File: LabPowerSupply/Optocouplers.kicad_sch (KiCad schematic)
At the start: 3 parts

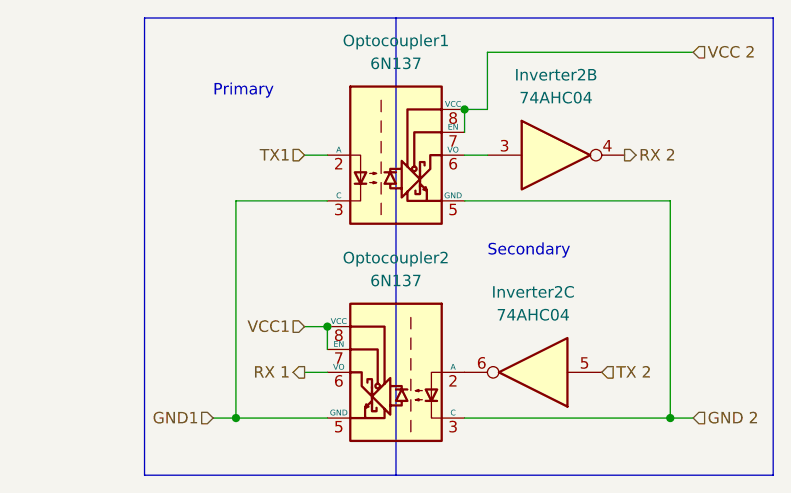
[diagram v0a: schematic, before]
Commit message: Fixed MCU communication pins and optocoupler
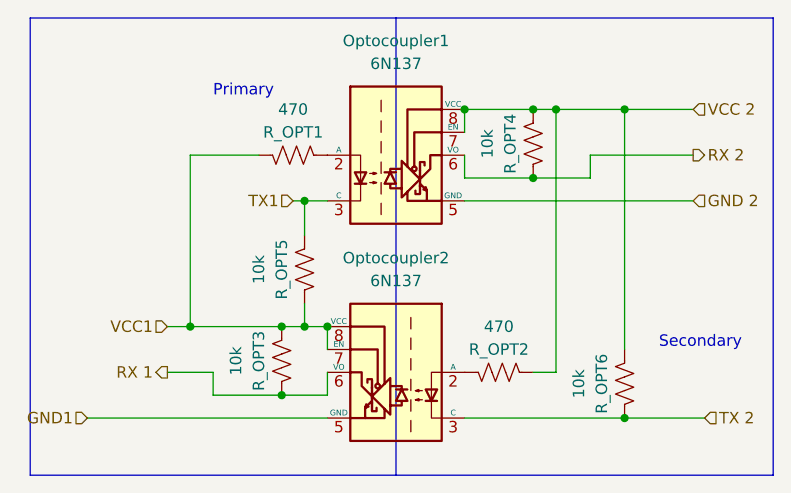
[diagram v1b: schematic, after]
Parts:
- removed Inverter2: 74AHC04, Package_SO:SSOP-14_5.3x6.2mm_P0.65mm, symbol 74xx:74AHC04
- added R_OPT1, R_OPT2: 470, Resistor_SMD:R_0603_1608Metric, symbol Device:R_US
- added R_OPT3, R_OPT4, R_OPT5, R_OPT6: 10k, Resistor_SMD:R_0603_1608Metric, symbol Device:R_US
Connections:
- net GND 2: no longer Optocoupler2.3 (C)
- net GND1: no longer Optocoupler1.3 (C)
- net RX 1: now also R_OPT3.1
- net RX 2: now also Optocoupler1.6 (VO), R_OPT4.1
- net TX 2: now also Optocoupler2.3 (C), R_OPT6.1
- net TX1: now also Optocoupler1.3 (C), R_OPT5.2; no longer Optocoupler1.2 (A)
- net VCC 2: now also R_OPT2.2, R_OPT4.2, R_OPT6.2
- net VCC1: now also R_OPT1.1, R_OPT3.2, R_OPT5.1
- net at Optocoupler2.2 (A): now also R_OPT2.1
- new net: Optocoupler1.2 (A), R_OPT1.2

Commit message: Began mcu placement
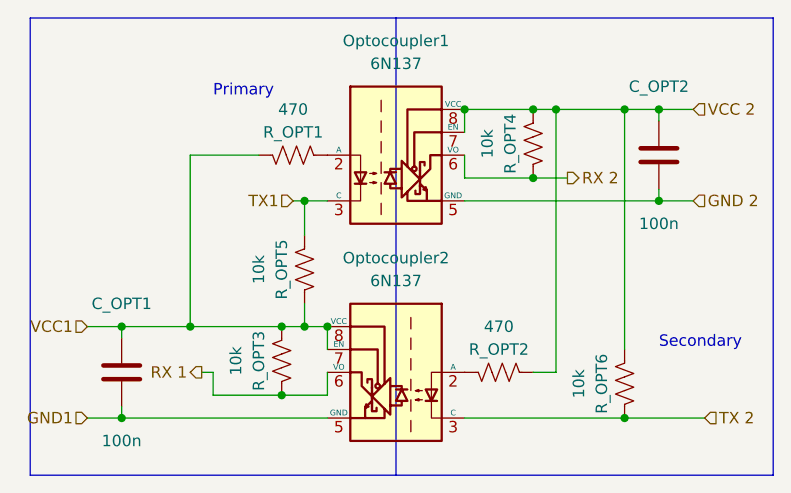
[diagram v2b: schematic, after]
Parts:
- added C_OPT1, C_OPT2: 100n, Capacitor_SMD:C_0603_1608Metric, symbol Device:C
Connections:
- net GND 2: now also C_OPT2.1
- net GND1: now also C_OPT1.1
- net VCC 2: now also C_OPT2.2
- net VCC1: now also C_OPT1.2
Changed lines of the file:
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@@
   (junction (at 101.6 101.6) (diameter 0) (color 0 0 0 0)
   )
+  (junction (at 142.24 77.47) (diameter 0) (color 0 0 0 0)
+  )
+  (junction (at 114.3 87.63) (diameter 0) (color 0 0 0 0)
+  )
+  (junction (at 93.98 101.6) (diameter 0) (color 0 0 0 0)
+  )
+  (junction (at 111.76 101.6) (diameter 0) (color 0 0 0 0)
+  )
+  (junction (at 149.86 111.76) (diameter 0) (color 0 0 0 0)
+  )
+  (junction (at 153.67 87.63) (diameter 0) (color 0 0 0 0)
+  )
   (junction (at 139.7 85.09) (diameter 0) (color 0 0 0 0)
   )
-  (junction (at 142.24 77.47) (diameter 0) (color 0 0 0 0)
-  )
-  (junction (at 114.3 87.63) (diameter 0) (color 0 0 0 0)
-  )
-  (junction (at 111.76 101.6) (diameter 0) (color 0 0 0 0)
-  )
-  (junction (at 149.86 111.76) (diameter 0) (color 0 0 0 0)
-  )
   (junction (at 114.3 101.6) (diameter 0) (color 0 0 0 0)
   )
@@
   (junction (at 111.76 109.22) (diameter 0) (color 0 0 0 0)
   )
+  (junction (at 93.98 111.76) (diameter 0) (color 0 0 0 0)
+  )
   (junction (at 132.08 77.47) (diameter 0) (color 0 0 0 0)
   )
   (junction (at 116.84 101.6) (diameter 0) (color 0 0 0 0)
   )
+  (junction (at 153.67 77.47) (diameter 0) (color 0 0 0 0)
+  )
   (wire (pts (xy 149.86 111.76) (xy 158.75 111.76))
     (stroke (width 0) (type default) (color 0 0 0 0))
@@
     (stroke (width 0) (type default) (color 0 0 0 0))
   )
+  (wire (pts (xy 153.67 77.47) (xy 157.48 77.47))
+    (stroke (width 0) (type default) (color 0 0 0 0))
+  )
   (wire (pts (xy 132.08 111.76) (xy 149.86 111.76))
     (stroke (width 0) (type default) (color 0 0 0 0))
@@
     (stroke (width 0) (type default) (color 0 0 0 0))
   )
-  (wire (pts (xy 90.17 111.76) (xy 116.84 111.76))
-    (stroke (width 0) (type default) (color 0 0 0 0))
-  )
-  (wire (pts (xy 99.06 101.6) (xy 101.6 101.6))
+  (wire (pts (xy 90.17 111.76) (xy 93.98 111.76))
+    (stroke (width 0) (type default) (color 0 0 0 0))
+  )
+  (wire (pts (xy 90.17 101.6) (xy 93.98 101.6))
     (stroke (width 0) (type default) (color 0 0 0 0))
   )
@@
     (stroke (width 0) (type default) (color 0 0 0 0))
   )
-  (wire (pts (xy 104.14 106.68) (xy 99.06 106.68))
+  (wire (pts (xy 104.14 106.68) (xy 102.87 106.68))
     (stroke (width 0) (type default) (color 0 0 0 0))
   )
@@
     (stroke (width 0) (type default) (color 0 0 0 0))
   )
-  (wire (pts (xy 146.05 82.55) (xy 157.48 82.55))
+  (wire (pts (xy 93.98 101.6) (xy 93.98 102.87))
     (stroke (width 0) (type default) (color 0 0 0 0))
   )
@@
     (stroke (width 0) (type default) (color 0 0 0 0))
   )
-  (wire (pts (xy 132.08 87.63) (xy 157.48 87.63))
+  (wire (pts (xy 153.67 77.47) (xy 153.67 78.74))
+    (stroke (width 0) (type default) (color 0 0 0 0))
+  )
+  (wire (pts (xy 132.08 87.63) (xy 153.67 87.63))
     (stroke (width 0) (type default) (color 0 0 0 0))
   )
@@
     (stroke (width 0) (type default) (color 0 0 0 0))
   )
-  (wire (pts (xy 149.86 77.47) (xy 157.48 77.47))
+  (wire (pts (xy 149.86 77.47) (xy 153.67 77.47))
     (stroke (width 0) (type default) (color 0 0 0 0))
   )
@@
     (stroke (width 0) (type default) (color 0 0 0 0))
   )
-  (wire (pts (xy 139.7 85.09) (xy 146.05 85.09))
+  (wire (pts (xy 93.98 110.49) (xy 93.98 111.76))
+    (stroke (width 0) (type default) (color 0 0 0 0))
+  )
+  (wire (pts (xy 139.7 85.09) (xy 143.51 85.09))
     (stroke (width 0) (type default) (color 0 0 0 0))
   )
@@
     (stroke (width 0) (type default) (color 0 0 0 0))
   )
+  (wire (pts (xy 153.67 86.36) (xy 153.67 87.63))
+    (stroke (width 0) (type default) (color 0 0 0 0))
+  )
   (wire (pts (xy 114.3 87.63) (xy 114.3 91.44))
     (stroke (width 0) (type default) (color 0 0 0 0))
   )
+  (wire (pts (xy 93.98 111.76) (xy 116.84 111.76))
+    (stroke (width 0) (type default) (color 0 0 0 0))
+  )
   (wire (pts (xy 132.08 77.47) (xy 139.7 77.47))
     (stroke (width 0) (type default) (color 0 0 0 0))
@@
     (stroke (width 0) (type default) (color 0 0 0 0))
   )
+  (wire (pts (xy 153.67 87.63) (xy 157.48 87.63))
+    (stroke (width 0) (type default) (color 0 0 0 0))
+  )
   (wire (pts (xy 101.6 101.6) (xy 111.76 101.6))
     (stroke (width 0) (type default) (color 0 0 0 0))
@@
     (stroke (width 0) (type default) (color 0 0 0 0))
   )
-  (wire (pts (xy 146.05 85.09) (xy 146.05 82.55))
-    (stroke (width 0) (type default) (color 0 0 0 0))
-  )
   (polyline (pts (xy 166.37 118.11) (xy 166.37 67.31))
+    (stroke (width 0) (type default) (color 0 0 0 0))
+  )
+  (wire (pts (xy 93.98 101.6) (xy 101.6 101.6))
     (stroke (width 0) (type default) (color 0 0 0 0))
   )
@@
     (effects (font (size 1.27 1.27)) (justify right))
   )
-  (hierarchical_label "RX 1" (shape output) (at 99.06 106.68 180)
+  (hierarchical_label "RX 1" (shape output) (at 102.87 106.68 180)
     (effects (font (size 1.27 1.27)) (justify right))
   )
@@
     (effects (font (size 1.27 1.27)) (justify left))
   )
-  (hierarchical_label "RX 2" (shape output) (at 157.48 82.55 0)
-    (effects (font (size 1.27 1.27)) (justify left))
-  )
-  (hierarchical_label "VCC1" (shape input) (at 99.06 101.6 180)
+  (hierarchical_label "RX 2" (shape output) (at 143.51 85.09 0)
+    (effects (font (size 1.27 1.27)) (justify left))
+  )
+  (hierarchical_label "VCC1" (shape input) (at 90.17 101.6 180)
     (effects (font (size 1.27 1.27)) (justify right))
   )
@@
     (pin "2")
   )
+  (symbol (lib_id "Device:C") (at 93.98 106.68 180) (unit 1)
+    (in_bom yes) (on_board yes)
+    (property "Reference" "C_OPT1" (id 0) (at 93.98 99.06 0))
+    (property "Value" "100n" (id 1) (at 93.98 114.3 0))
+    (property "Footprint" "Capacitor_SMD:C_0603_1608Metric" (id 2) (at 93.0148 102.87 0)
+      (effects (font (size 1.27 1.27)) hide)
+    )
+    (property "Datasheet" "~" (id 3) (at 93.98 106.68 0)
+      (effects (font (size 1.27 1.27)) hide)
+    )
+    (pin "1")
+    (pin "2")
+  )
   (symbol (lib_id "Device:R_US") (at 114.3 95.25 0) (mirror x) (unit 1)
     (in_bom yes) (on_board yes)
@@
       (effects (font (size 1.27 1.27)) hide)
     )
+    (pin "1")
+    (pin "2")
+  )
+  (symbol (lib_id "Device:C") (at 153.67 82.55 180) (unit 1)
+    (in_bom yes) (on_board yes)
+    (property "Reference" "C_OPT2" (id 0) (at 153.67 74.93 0))
+    (property "Value" "100n" (id 1) (at 153.67 90.17 0))
+    (property "Footprint" "Capacitor_SMD:C_0603_1608Metric" (id 2) (at 152.7048 78.74 0)
+      (effects (font (size 1.27 1.27)) hide)
+    )
+    (property "Datasheet" "~" (id 3) (at 153.67 82.55 0)
+      (effects (font (size 1.27 1.27)) hide)
+    )

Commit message: Updated Part List
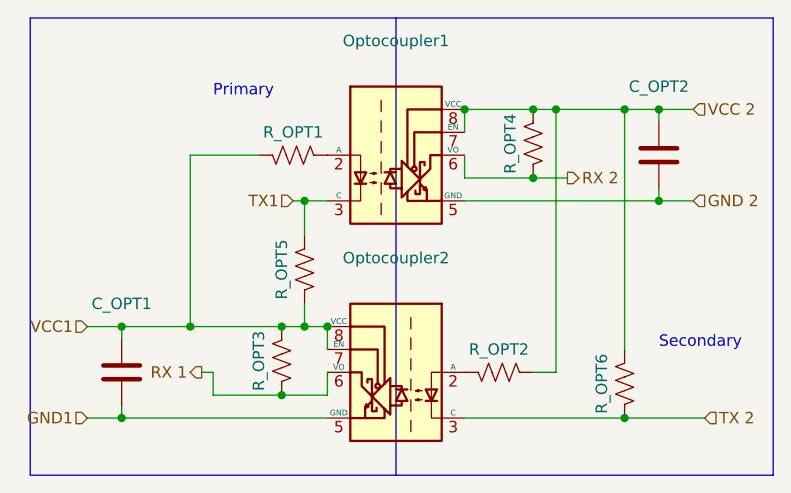
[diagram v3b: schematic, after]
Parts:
- C_OPT1, C_OPT2: value 100n -> (none); footprint Capacitor_SMD:C_0603_1608Metric -> (none)
- Optocoupler1, Optocoupler2: value 6N137 -> (none); footprint Package_DIP:PowerIntegrations_SMD-8 -> (none)
- R_OPT1, R_OPT2: value 470 -> (none); footprint Resistor_SMD:R_0603_1608Metric -> (none)
- R_OPT3, R_OPT4, R_OPT5, R_OPT6: value 10k -> (none); footprint Resistor_SMD:R_0603_1608Metric -> (none)
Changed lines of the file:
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@@
     (in_bom yes) (on_board yes)
     (property "Reference" "R_OPT3" (id 0) (at 109.22 105.41 90))
-    (property "Value" "10k" (id 1) (at 106.68 105.41 90))
-    (property "Footprint" "Resistor_SMD:R_0603_1608Metric" (id 2) (at 112.776 105.156 90)
+    (property "Value" "" (id 1) (at 106.68 105.41 90))
+    (property "Footprint" "" (id 2) (at 112.776 105.156 90)
       (effects (font (size 1.27 1.27)) hide)
     )
@@
     (in_bom yes) (on_board yes)
     (property "Reference" "R_OPT2" (id 0) (at 135.89 104.14 90))
-    (property "Value" "470" (id 1) (at 135.89 101.6 90))
-    (property "Footprint" "Resistor_SMD:R_0603_1608Metric" (id 2) (at 136.144 107.696 90)
+    (property "Value" "" (id 1) (at 135.89 101.6 90))
+    (property "Footprint" "" (id 2) (at 136.144 107.696 90)
       (effects (font (size 1.27 1.27)) hide)
     )
@@
     (in_bom yes) (on_board yes)
     (property "Reference" "C_OPT1" (id 0) (at 93.98 99.06 0))
-    (property "Value" "100n" (id 1) (at 93.98 114.3 0))
-    (property "Footprint" "Capacitor_SMD:C_0603_1608Metric" (id 2) (at 93.0148 102.87 0)
+    (property "Value" "" (id 1) (at 93.98 114.3 0))
+    (property "Footprint" "" (id 2) (at 93.0148 102.87 0)
       (effects (font (size 1.27 1.27)) hide)
     )
@@
     (in_bom yes) (on_board yes)
     (property "Reference" "R_OPT5" (id 0) (at 111.76 95.25 90))
-    (property "Value" "10k" (id 1) (at 109.22 95.25 90))
-    (property "Footprint" "Resistor_SMD:R_0603_1608Metric" (id 2) (at 115.316 94.996 90)
+    (property "Value" "" (id 1) (at 109.22 95.25 90))
+    (property "Footprint" "" (id 2) (at 115.316 94.996 90)
       (effects (font (size 1.27 1.27)) hide)
     )
@@
     (in_bom yes) (on_board yes)
     (property "Reference" "C_OPT2" (id 0) (at 153.67 74.93 0))
-    (property "Value" "100n" (id 1) (at 153.67 90.17 0))
-    (property "Footprint" "Capacitor_SMD:C_0603_1608Metric" (id 2) (at 152.7048 78.74 0)
+    (property "Value" "" (id 1) (at 153.67 90.17 0))
+    (property "Footprint" "" (id 2) (at 152.7048 78.74 0)
       (effects (font (size 1.27 1.27)) hide)
     )
@@
     (in_bom yes) (on_board yes)
     (property "Reference" "R_OPT6" (id 0) (at 147.32 107.95 90))
-    (property "Value" "10k" (id 1) (at 144.78 107.95 90))
-    (property "Footprint" "Resistor_SMD:R_0603_1608Metric" (id 2) (at 150.876 107.696 90)
+    (property "Value" "" (id 1) (at 144.78 107.95 90))
+    (property "Footprint" "" (id 2) (at 150.876 107.696 90)
       (effects (font (size 1.27 1.27)) hide)
     )
@@
     (in_bom yes) (on_board yes)
     (property "Reference" "R_OPT4" (id 0) (at 137.16 81.28 90))
-    (property "Value" "10k" (id 1) (at 134.62 81.28 90))
-    (property "Footprint" "Resistor_SMD:R_0603_1608Metric" (id 2) (at 140.716 81.026 90)
+    (property "Value" "" (id 1) (at 134.62 81.28 90))
+    (property "Footprint" "" (id 2) (at 140.716 81.026 90)
       (effects (font (size 1.27 1.27)) hide)
     )
@@
     (in_bom yes) (on_board yes)
     (property "Reference" "R_OPT1" (id 0) (at 113.03 80.01 90))
-    (property "Value" "470" (id 1) (at 113.03 77.47 90))
-    (property "Footprint" "Resistor_SMD:R_0603_1608Metric" (id 2) (at 113.284 83.566 90)
+    (property "Value" "" (id 1) (at 113.03 77.47 90))
+    (property "Footprint" "" (id 2) (at 113.284 83.566 90)
       (effects (font (size 1.27 1.27)) hide)
     )
@@
     (in_bom yes) (on_board yes) (fields_autoplaced)
     (property "Reference" "Optocoupler2" (id 0) (at 124.46 93.98 0))
-    (property "Value" "6N137" (id 1) (at 124.46 96.52 0))
-    (property "Footprint" "Package_DIP:PowerIntegrations_SMD-8" (id 2) (at 124.46 119.38 0)
+    (property "Value" "" (id 1) (at 124.46 96.52 0))
+    (property "Footprint" "" (id 2) (at 124.46 119.38 0)
       (effects (font (size 1.27 1.27)) hide)
     )
@@
     (in_bom yes) (on_board yes) (fields_autoplaced)
     (property "Reference" "Optocoupler1" (id 0) (at 124.46 69.85 0))
-    (property "Value" "6N137" (id 1) (at 124.46 72.39 0))
-    (property "Footprint" "Package_DIP:PowerIntegrations_SMD-8" (id 2) (at 124.46 95.25 0)
+    (property "Value" "" (id 1) (at 124.46 72.39 0))
+    (property "Footprint" "" (id 2) (at 124.46 95.25 0)
       (effects (font (size 1.27 1.27)) hide)
     )
